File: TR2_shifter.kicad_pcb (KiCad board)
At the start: 2 copper layers, 69.2 x 29.8 mm, 28 parts, among them U1 LM339_DIP, U2 LM339_DIP

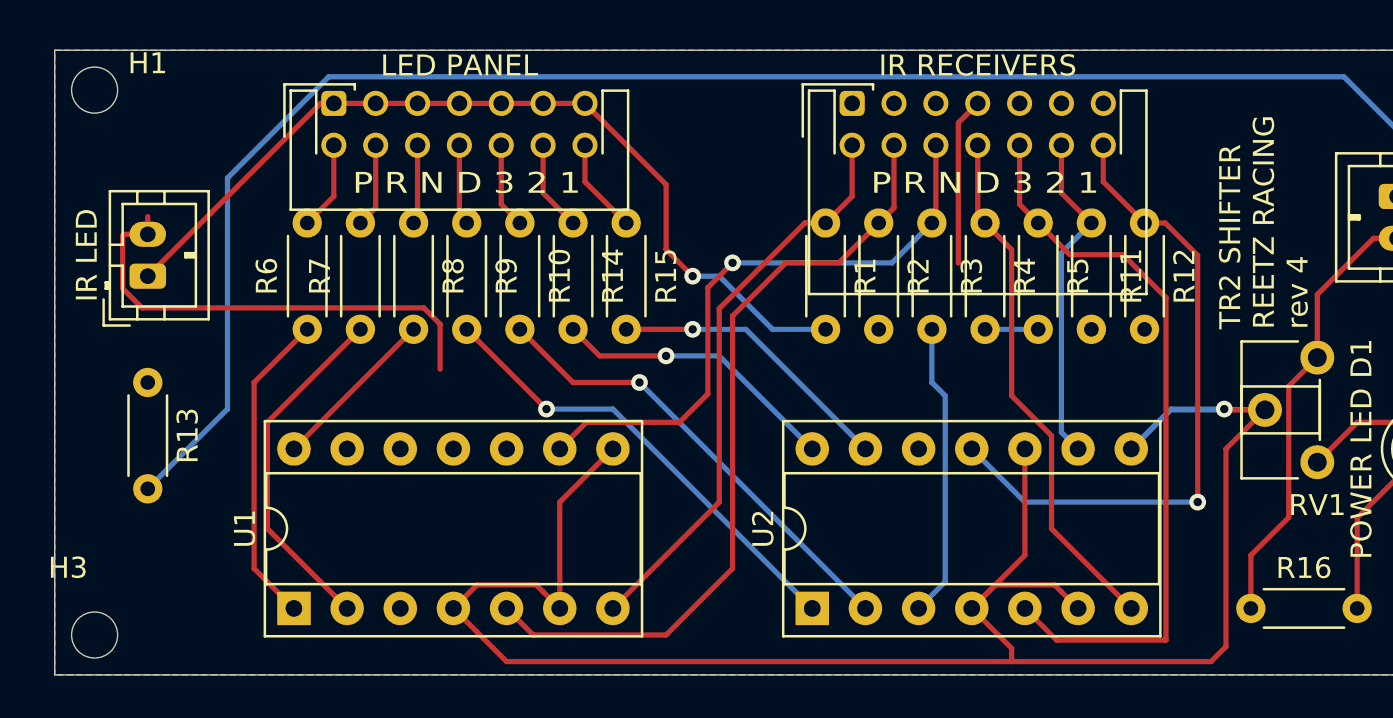
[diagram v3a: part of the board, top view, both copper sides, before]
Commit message: Move U1 and U2 for more unified ground/power plane
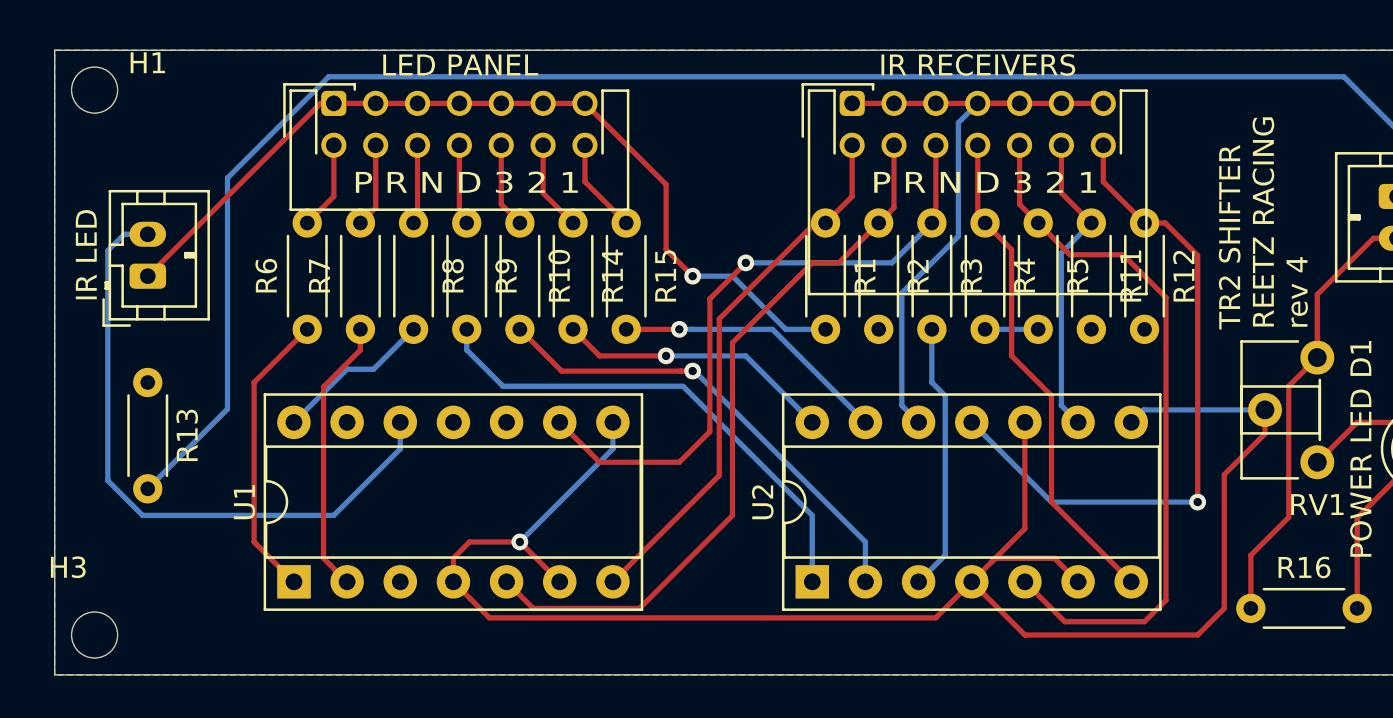
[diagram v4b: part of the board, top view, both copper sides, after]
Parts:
- moved U1 1.27 mm to (163.2, 94.0)
- moved U2 1.27 mm to (188.0, 94.0)
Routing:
- net GND: track 51.9 -> 82.8 mm
- net REF_V: track 97.4 -> 85.0 mm
- net Net-(R7-Pad1): track 16.8 -> 13.3 mm
- net REV_IR: track 37.5 -> 34.8 mm
- net Net-(R9-Pad2): track 22.0 -> 23.9 mm, vias 1 -> 0
- net NEU_IR: track 29.0 -> 30.8 mm
- net PARK_IR: track 27.4 -> 25.9 mm
- net 3_IR: track 35.4 -> 34.1 mm
- net Net-(R6-Pad1): track 15.2 -> 13.9 mm
- net DRIVE_IR: track 25.2 -> 23.9 mm
- net 2_IR: track 16.0 -> 14.8 mm
- net +5V: track 64.6 -> 63.4 mm
- net Net-(R10-Pad2): track 22.0 -> 22.8 mm
- net 1_IR: track 31.3 -> 31.9 mm
- net Net-(R8-Pad2): track 8.08 -> 7.56 mm
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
